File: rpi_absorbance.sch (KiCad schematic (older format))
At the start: 33 parts, among them CON1 BARREL_JACK, P1 CONN_02X04, P2 CONN_01X02, P3 RPI_HEADER, P4 STEPPER_CONN, P5 CONN_02X06, Q1 ZTX692B, U1 R-78B5.0-1.5L, U2 NXP_PUMH10, U3 DRV8825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

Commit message: Reorganize project
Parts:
- CON1: footprint footprints:CUI_PJ-002AH-SMT -> jnod_footprints:CUI_PJ-002AH-SMT
- D1: footprint footprints:SOD-123 -> jnod_footprints:SOD-123
- RV1, RV2: footprint footprints:BOURNS_TC33 -> jnod_footprints:BOURNS_TC33
- U1: footprint footprints:R-78B-3-SIP -> jnod_footprints:R-78B-3-SIP
- U2: footprint footprints:SOT−363 -> jnod_footprints:SOT−363
- U3: footprint footprints:28-HTSSOP -> jnod_footprints:28-HTSSOP
- U4: footprint footprints:8-VSSOP -> jnod_footprints:8-VSSOP
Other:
- note added: "Device Connectors"
- note removed: "Device Connector"
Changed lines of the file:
@@
 F 0 "U3" H 6800 4750 60  0000 C CNN
 F 1 "DRV8825" H 6500 4750 60  0000 C CNN
-F 2 "footprints:28-HTSSOP" H 5850 3750 60  0001 C CNN
+F 2 "jnod_footprints:28-HTSSOP" H 5850 3750 60  0001 C CNN
 F 3 "" H 5850 3750 60  0000 C CNN
 	1    6700 4000
@@
 F 0 "U1" H 2850 2100 60  0000 C CNN
 F 1 "R-78B5.0-1.5L" H 2950 2500 60  0000 C CNN
-F 2 "footprints:R-78B-3-SIP" H 2750 2550 60  0001 C CNN
+F 2 "jnod_footprints:R-78B-3-SIP" H 2750 2550 60  0001 C CNN
 F 3 "" H 2750 2550 60  0000 C CNN
 	1    2750 2300
@@
 F 0 "U4" H 4850 2000 60  0000 C CNN
 F 1 "TCA9406DCUR" H 4850 2500 60  0000 C CNN
-F 2 "footprints:8-VSSOP" H 4900 2600 60  0001 C CNN
+F 2 "jnod_footprints:8-VSSOP" H 4900 2600 60  0001 C CNN
 F 3 "" H 4900 2600 60  0000 C CNN
 	1    4850 2250
@@
 L PWR_FLAG #FLG021
 U 1 1 56CC8492
-P 900 6400
-F 0 "#FLG021" H 900 6495 50  0001 C CNN
-F 1 "PWR_FLAG" H 900 6580 50  0000 C CNN
-F 2 "" H 900 6400 50  0000 C CNN
-F 3 "" H 900 6400 50  0000 C CNN
-	1    900  6400
+P 1450 6400
+F 0 "#FLG021" H 1450 6495 50  0001 C CNN
+F 1 "PWR_FLAG" H 1450 6580 50  0000 C CNN
+F 2 "" H 1450 6400 50  0000 C CNN
+F 3 "" H 1450 6400 50  0000 C CNN
+	1    1450 6400
 	1    0    0    -1
 $EndComp
@@
 L +5V #PWR022
 U 1 1 56CC84E3
-P 900 6450
-F 0 "#PWR022" H 900 6300 50  0001 C CNN
-F 1 "+5V" H 900 6590 50  0000 C CNN
-F 2 "" H 900 6450 50  0000 C CNN
-F 3 "" H 900 6450 50  0000 C CNN
-	1    900  6450
+P 1450 6450
+F 0 "#PWR022" H 1450 6300 50  0001 C CNN
+F 1 "+5V" H 1450 6590 50  0000 C CNN
+F 2 "" H 1450 6450 50  0000 C CNN
+F 3 "" H 1450 6450 50  0000 C CNN
+	1    1450 6450
 	-1   0    0    1
 $EndComp
@@
 L +12V #PWR023
 U 1 1 56CC852D
-P 1400 6450
-F 0 "#PWR023" H 1400 6300 50  0001 C CNN
-F 1 "+12V" H 1400 6590 50  0000 C CNN
-F 2 "" H 1400 6450 50  0000 C CNN
-F 3 "" H 1400 6450 50  0000 C CNN
-	1    1400 6450
+P 1950 6450
+F 0 "#PWR023" H 1950 6300 50  0001 C CNN
+F 1 "+12V" H 1950 6590 50  0000 C CNN
+F 2 "" H 1950 6450 50  0000 C CNN
+F 3 "" H 1950 6450 50  0000 C CNN
+	1    1950 6450
 	-1   0    0    1
 $EndComp
@@
 L GND #PWR024
 U 1 1 56CC8577
-P 900 6950
-F 0 "#PWR024" H 900 6700 50  0001 C CNN
-F 1 "GND" H 900 6800 50  0000 C CNN
-F 2 "" H 900 6950 50  0000 C CNN
-F 3 "" H 900 6950 50  0000 C CNN
-	1    900  6950
+P 1450 6950
+F 0 "#PWR024" H 1450 6700 50  0001 C CNN
+F 1 "GND" H 1450 6800 50  0000 C CNN
+F 2 "" H 1450 6950 50  0000 C CNN
+F 3 "" H 1450 6950 50  0000 C CNN
+	1    1450 6950
 	1    0    0    -1
 $EndComp
@@
 L +3.3V #PWR025
 U 1 1 56CC85C1
-P 1400 6950
-F 0 "#PWR025" H 1400 6800 50  0001 C CNN
-F 1 "+3.3V" H 1400 7090 50  0000 C CNN
-F 2 "" H 1400 6950 50  0000 C CNN
-F 3 "" H 1400 6950 50  0000 C CNN
-	1    1400 6950
+P 1950 6950
+F 0 "#PWR025" H 1950 6800 50  0001 C CNN
+F 1 "+3.3V" H 1950 7090 50  0000 C CNN
+F 2 "" H 1950 6950 50  0000 C CNN
+F 3 "" H 1950 6950 50  0000 C CNN
+	1    1950 6950
 	-1   0    0    1
 $EndComp
@@
 L PWR_FLAG #FLG026
 U 1 1 56CC860B
-P 1400 6400
-F 0 "#FLG026" H 1400 6495 50  0001 C CNN
-F 1 "PWR_FLAG" H 1400 6580 50  0000 C CNN
-F 2 "" H 1400 6400 50  0000 C CNN
-F 3 "" H 1400 6400 50  0000 C CNN
-	1    1400 6400
+P 1950 6400
+F 0 "#FLG026" H 1950 6495 50  0001 C CNN
+F 1 "PWR_FLAG" H 1950 6580 50  0000 C CNN
+F 2 "" H 1950 6400 50  0000 C CNN
+F 3 "" H 1950 6400 50  0000 C CNN
+	1    1950 6400
 	1    0    0    -1
 $EndComp
@@
 L PWR_FLAG #FLG027
 U 1 1 56CC8655
-P 900 6900
-F 0 "#FLG027" H 900 6995 50  0001 C CNN
-F 1 "PWR_FLAG" H 900 7080 50  0000 C CNN
-F 2 "" H 900 6900 50  0000 C CNN
-F 3 "" H 900 6900 50  0000 C CNN
-	1    900  6900
+P 1450 6900
+F 0 "#FLG027" H 1450 6995 50  0001 C CNN
+F 1 "PWR_FLAG" H 1450 7080 50  0000 C CNN
+F 2 "" H 1450 6900 50  0000 C CNN
+F 3 "" H 1450 6900 50  0000 C CNN
+	1    1450 6900
 	1    0    0    -1
 $EndComp
@@
 L PWR_FLAG #FLG028
 U 1 1 56CC88FF
-P 1400 6900
-F 0 "#FLG028" H 1400 6995 50  0001 C CNN
-F 1 "PWR_FLAG" H 1400 7080 50  0000 C CNN
-F 2 "" H 1400 6900 50  0000 C CNN
-F 3 "" H 1400 6900 50  0000 C CNN
-	1    1400 6900
+P 1950 6900
+F 0 "#FLG028" H 1950 6995 50  0001 C CNN
+F 1 "PWR_FLAG" H 1950 7080 50  0000 C CNN
+F 2 "" H 1950 6900 50  0000 C CNN
+F 3 "" H 1950 6900 50  0000 C CNN
+	1    1950 6900
 	1    0    0    -1
 $EndComp
@@
 F 0 "RV1" H 5850 4620 50  0000 C CNN
 F 1 "POT" H 5850 4700 50  0000 C CNN
-F 2 "footprints:BOURNS_TC33" H 5850 4700 50  0001 C CNN
+F 2 "jnod_footprints:BOURNS_TC33" H 5850 4700 50  0001 C CNN
 F 3 "" H 5850 4700 50  0000 C CNN
 	1    5850 4700
@@
 F 0 "CON1" H 1500 2450 50  0000 C CNN
 F 1 "BARREL_JACK" H 1400 2000 50  0000 C CNN
-F 2 "footprints:CUI_PJ-002AH-SMT" H 1500 2200 50  0001 C CNN
+F 2 "jnod_footprints:CUI_PJ-002AH-SMT" H 1500 2200 50  0001 C CNN
 F 3 "" H 1500 2200 50  0000 C CNN
 	1    1500 2200
@@
 F 0 "D1" H 6000 6100 50  0000 C CNN
 F 1 "D" H 6000 5900 50  0000 C CNN
-F 2 "footprints:SOD-123" H 6000 6000 50  0001 C CNN
+F 2 "jnod_footprints:SOD-123" H 6000 6000 50  0001 C CNN
 F 3 "" H 6000 6000 50  0000 C CNN
 	1    6000 6000
@@
 F 0 "RV2" H 5250 6420 50  0000 C CNN
 F 1 "POT" H 5250 6500 50  0000 C CNN
-F 2 "footprints:BOURNS_TC33" H 5250 6500 50  0001 C CNN
+F 2 "jnod_footprints:BOURNS_TC33" H 5250 6500 50  0001 C CNN
 F 3 "" H 5250 6500 50  0000 C CNN
 	1    5250 6500
@@
 $EndComp
 Text Notes 1200 2800 0    60   ~ 0
-Device Connector
+Device Connectors
 Text Notes 5100 5550 0    60   ~ 0
 Peristaltic Pump Driver
@@
 	2750 5650 3100 5650
 Wire Wire Line
-	1400 6400 1400 6450
-Wire Wire Line
-	900  6400 900  6450
-Wire Wire Line
-	900  6900 900  6950
-Wire Wire Line
-	1400 6900 1400 6950
+	1950 6400 1950 6450
+Wire Wire Line
+	1450 6400 1450 6450
+Wire Wire Line
+	1450 6900 1450 6950
+Wire Wire Line
+	1950 6900 1950 6950
 Wire Notes Line
 	2400 5850 1100 5850
@@
 F 0 "U2" H 1950 3150 60  0000 C CNN
 F 1 "NXP_PUMH10" H 1950 3800 60  0000 C CNN
-F 2 "footprints:SOT−363" H 1950 3800 60  0001 C CNN
+F 2 "jnod_footprints:SOT−363" H 1950 3800 60  0001 C CNN
 F 3 "" H 1950 3800 60  0000 C CNN
 	1    1950 3450
 	1    0    0    -1
 $EndComp
+Wire Notes Line
+	4200 2700 4200 4800
 $EndSCHEMATC

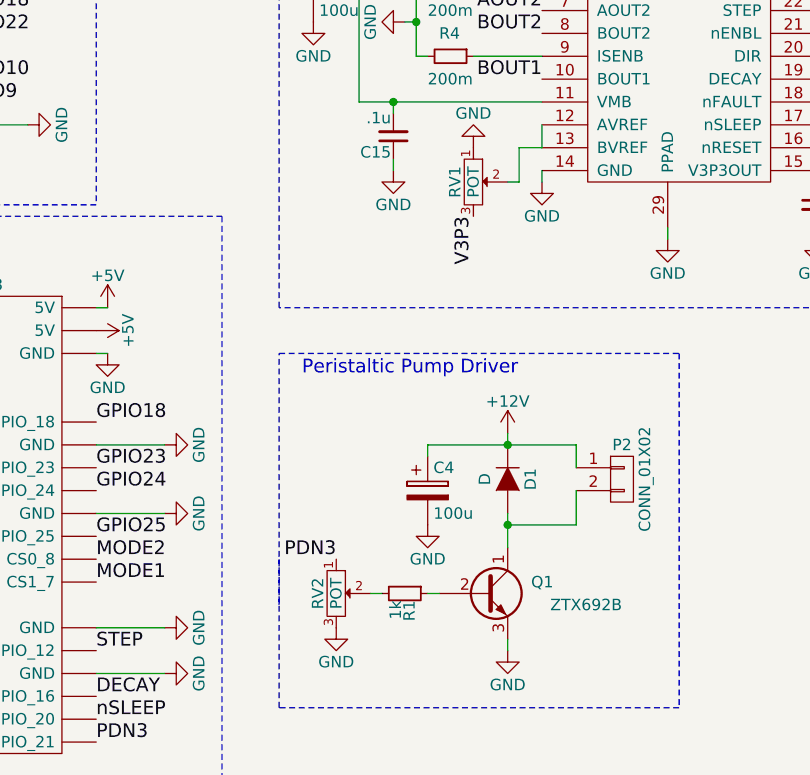
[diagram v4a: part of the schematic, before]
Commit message: Update footprints
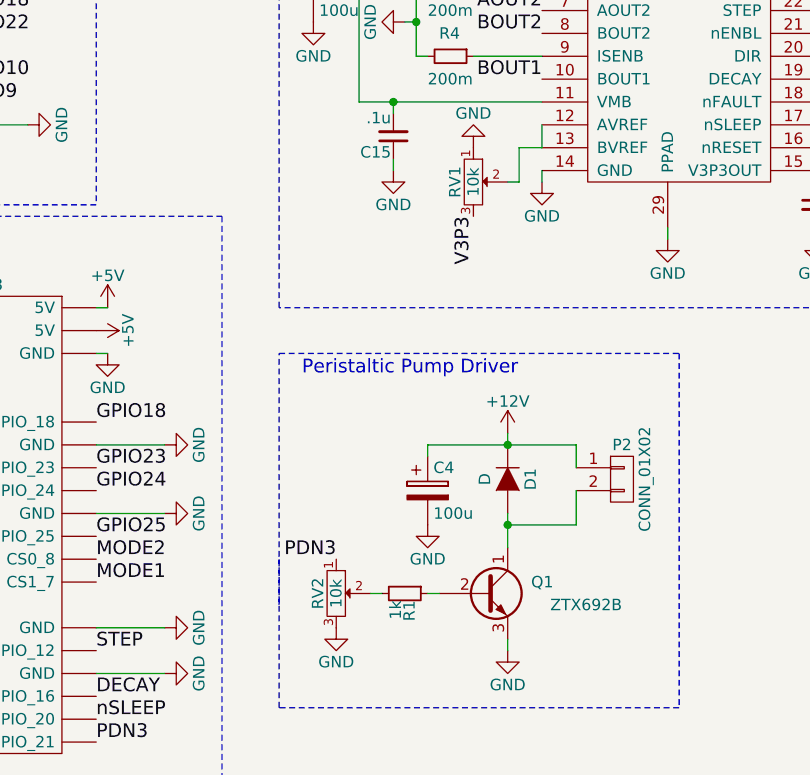
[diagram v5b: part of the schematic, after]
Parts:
- D1: footprint jnod_footprints:SOD-123 -> jnod_footprints:SOD-123_diode
- RV1, RV2: value POT -> 10k
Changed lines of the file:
@@
 P 5850 4700
 F 0 "RV1" H 5850 4620 50  0000 C CNN
-F 1 "POT" H 5850 4700 50  0000 C CNN
+F 1 "10k" H 5850 4700 50  0000 C CNN
 F 2 "jnod_footprints:BOURNS_TC33" H 5850 4700 50  0001 C CNN
 F 3 "" H 5850 4700 50  0000 C CNN
@@
 F 0 "D1" H 6000 6100 50  0000 C CNN
 F 1 "D" H 6000 5900 50  0000 C CNN
-F 2 "jnod_footprints:SOD-123" H 6000 6000 50  0001 C CNN
+F 2 "jnod_footprints:SOD-123_diode" H 6000 6000 50  0001 C CNN
 F 3 "" H 6000 6000 50  0000 C CNN
 	1    6000 6000
@@
 P 5250 6500
 F 0 "RV2" H 5250 6420 50  0000 C CNN
-F 1 "POT" H 5250 6500 50  0000 C CNN
+F 1 "10k" H 5250 6500 50  0000 C CNN
 F 2 "jnod_footprints:BOURNS_TC33" H 5250 6500 50  0001 C CNN
 F 3 "" H 5250 6500 50  0000 C CNN

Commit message: Update resistors
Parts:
- R1, R7, R8: footprint Resistors_SMD:R_0805_HandSoldering -> Resistors_SMD:R_0603_HandSoldering
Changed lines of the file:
@@
 F 0 "R8" H 5380 1970 50  0000 L CNN
 F 1 "10k" H 5380 1910 50  0000 L CNN
-F 2 "Resistors_SMD:R_0805_HandSoldering" H 5350 1950 50  0001 C CNN
+F 2 "Resistors_SMD:R_0603_HandSoldering" H 5350 1950 50  0001 C CNN
 F 3 "" H 5350 1950 50  0000 C CNN
 	1    5350 1950
@@
 F 0 "R7" H 4380 1970 50  0000 L CNN
 F 1 "10k" H 4380 1910 50  0000 L CNN
-F 2 "Resistors_SMD:R_0805_HandSoldering" H 4350 1950 50  0001 C CNN
+F 2 "Resistors_SMD:R_0603_HandSoldering" H 4350 1950 50  0001 C CNN
 F 3 "" H 4350 1950 50  0000 C CNN
 	1    4350 1950
@@
 F 0 "R1" H 5580 6520 50  0000 L CNN
 F 1 "1k" H 5580 6460 50  0000 L CNN
-F 2 "Resistors_SMD:R_0805_HandSoldering" H 5550 6500 50  0001 C CNN
+F 2 "Resistors_SMD:R_0603_HandSoldering" H 5550 6500 50  0001 C CNN
 F 3 "" H 5550 6500 50  0000 C CNN
 	1    5550 6500
